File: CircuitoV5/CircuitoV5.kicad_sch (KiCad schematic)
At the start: 8 parts, among them U1 LM324

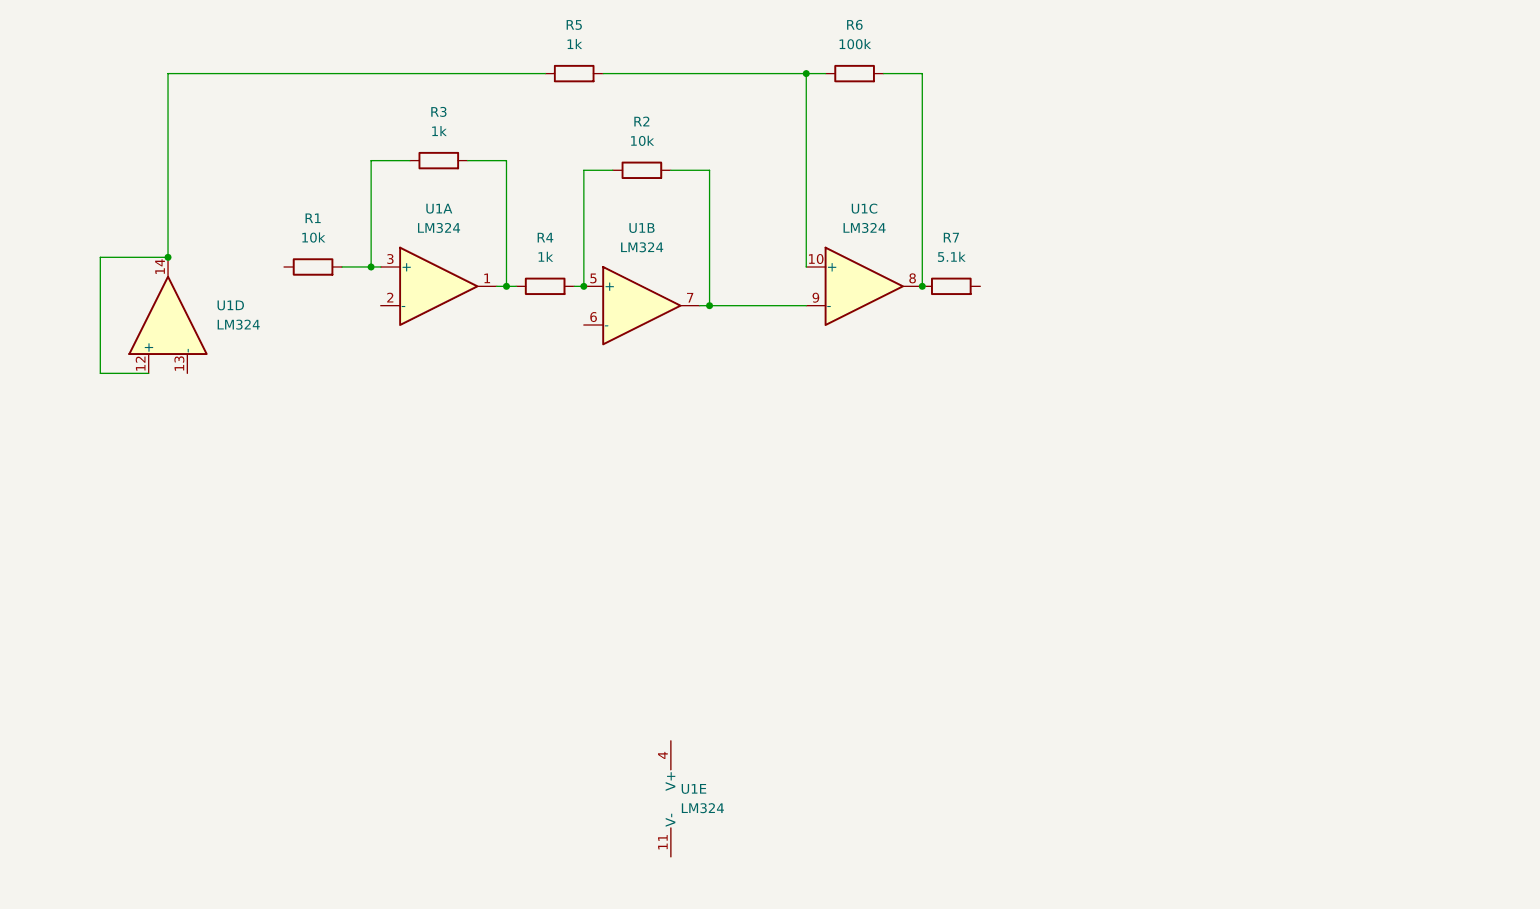
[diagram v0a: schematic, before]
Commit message: Schematic hecha, enrutado V1 planteado y empezado
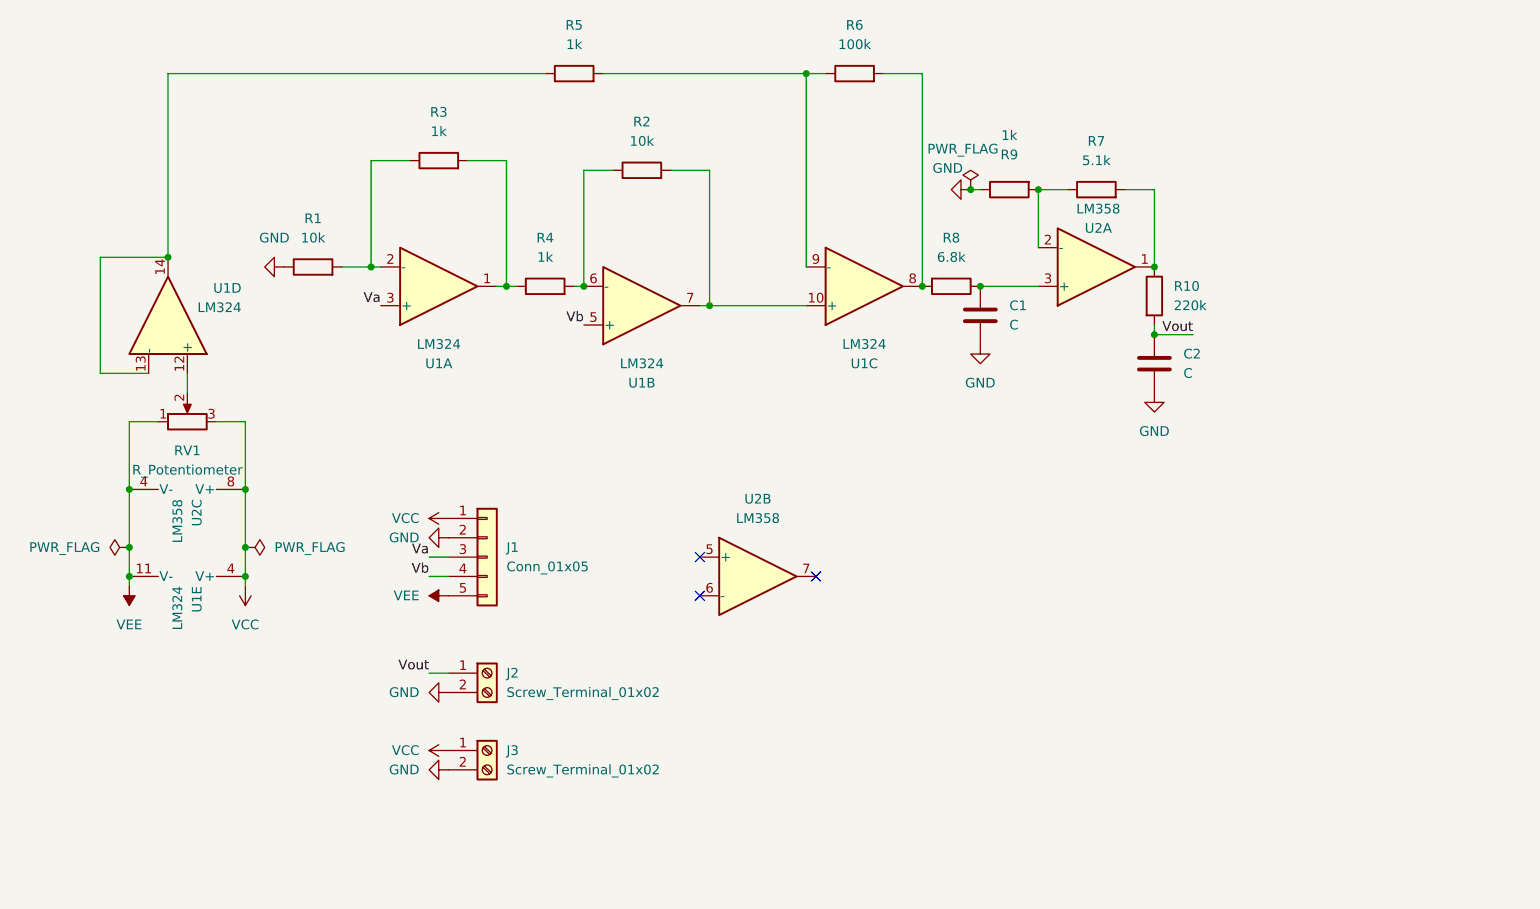
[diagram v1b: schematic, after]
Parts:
- added C1, C2: C, footprints:C_Rect_L9.5mm_W4.5mm_P5.00mm_MKT, symbol Device:C
- added J1: Conn_01x05, Connector_PinSocket_2.54mm:PinSocket_1x05_P2.54mm_Vertical, symbol Connector_Generic:Conn_01x05
- added J2, J3: Screw_Terminal_01x02, TerminalBlock_Phoenix:TerminalBlock_Phoenix_MKDS-1,5-2-5.08_1x02_P5.08mm_Horizontal, symbol Connector:Screw_Terminal_01x02
- added R10: 220k, Resistor_SMD:R_0201_0603Metric, symbol Device:R
- added R8: 6.8k, Resistor_SMD:R_0201_0603Metric, symbol Device:R
- added R9: 1k, Resistor_SMD:R_0603_1608Metric, symbol Device:R
- added RV1: R_Potentiometer, Potentiometer_THT:Potentiometer_Bourns_3296W_Vertical, symbol Device:R_Potentiometer
- added U2: LM358, footprints:DIP794W45P254L959H508Q8, symbol Amplifier_Operational:LM358
- U1: footprint (none) -> Package_SO:SOIC-14_3.9x8.7mm_P1.27mm; LCSC_Id C7943 -> C71035
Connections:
- net at R5.2, R6.1: now also U1.9 (-); no longer U1.10 (+)
- net at R6.2, U1.8: now also R8.2; no longer R7.1
- net at R2.2, U1.7: now also U1.10 (+); no longer U1.9 (-)
- net at U1.2 (-): now also R1.2, R3.1
- net at R5.1, U1.14: now also U1.13 (-); no longer U1.12 (+)
- net GND: now reaches R1.1
- net GND: now also C1.2, C2.2, J1.2 (Pin_2), J2.2 (Pin_2), J3.2 (Pin_2), R9.1
- net at R7.2: now also R10.1, U2.1
- net VEE: now reaches U1.11 (V-)
- net VEE: now also J1.5 (Pin_5), RV1.1, U2.4 (V-)
- net VCC: now reaches U1.4 (V+)
- net VCC: now also J1.1 (Pin_1), J3.1 (Pin_1), RV1.3, U2.8 (V+)
- net at R2.1, R4.2: now also U1.6 (-); no longer U1.5 (+)
- new net: R7.1, R9.2, U2.2 (-)
- new net: C1.1, R8.1, U2.3 (+)
- new net: RV1.2, U1.12 (+)
- new net Va: J1.3 (Pin_3), U1.3 (+)
- new net Vb: J1.4 (Pin_4), U1.5 (+)
- new net Vout: C2.1, J2.1 (Pin_1), R10.2
- no-connect marks 0 -> 3
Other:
- moved on the sheet: R7, U1D, U1E

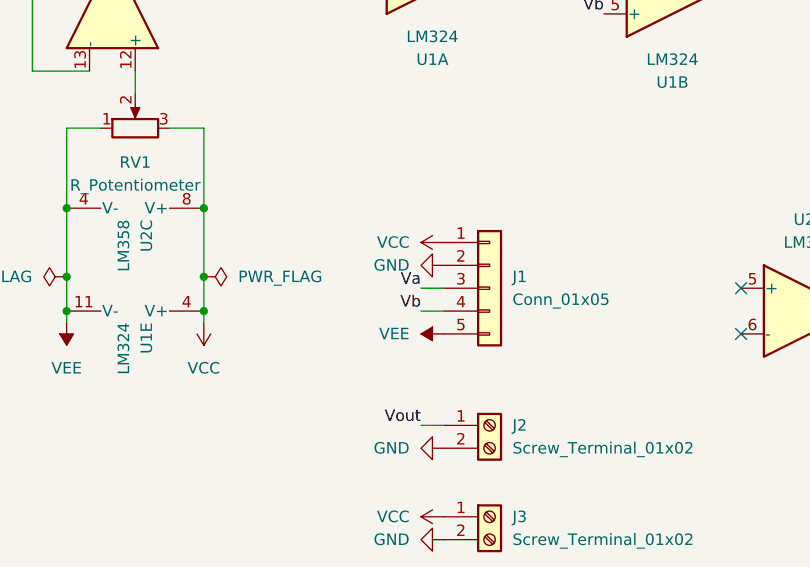
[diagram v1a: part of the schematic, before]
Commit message: componentes añadidos y proyecto ligeramente reordenado
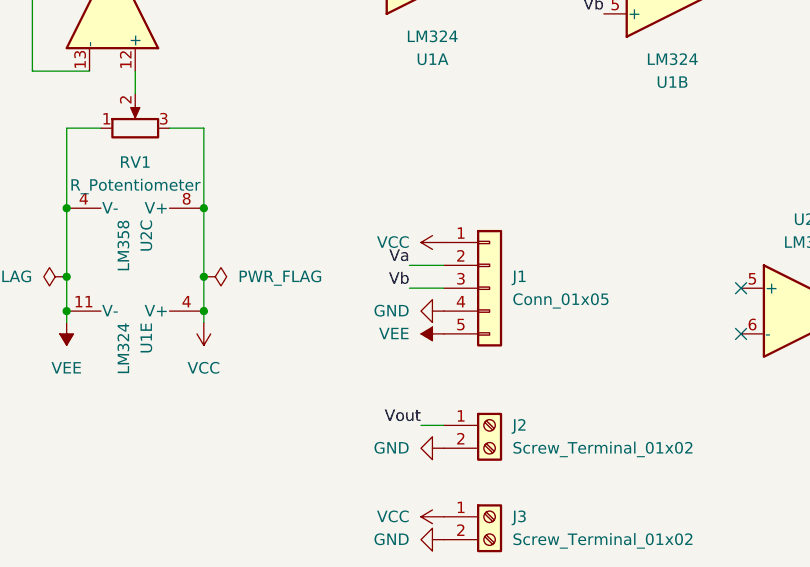
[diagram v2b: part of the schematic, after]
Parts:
- J1: footprint Connector_PinSocket_2.54mm:PinSocket_1x05_P2.54mm_Vertical -> Connector_PinSocket_2.54mm:PinSocket_1x05_P2.54mm_Horizontal
- U1: footprint Package_SO:SOIC-14_3.9x8.7mm_P1.27mm -> easyeda2kicad:PDIP-14_L19.7-W6.6-P2.54-LS8.3-BL
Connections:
- net GND: now also J1.4 (Pin_4); no longer J1.2 (Pin_2)
- net Va: now also J1.2 (Pin_2); no longer J1.3 (Pin_3)
- net Vb: now also J1.3 (Pin_3); no longer J1.4 (Pin_4)
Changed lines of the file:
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@@
 	(wire
 		(pts
-			(xy 86.36 91.44) (xy 88.9 91.44)
+			(xy 135.89 27.94) (xy 135.89 53.34)
 		)
 		(stroke
@@
 	(wire
 		(pts
-			(xy 135.89 27.94) (xy 135.89 53.34)
+			(xy 85.09 88.9) (xy 88.9 88.9)
 		)
 		(stroke
@@
 	(wire
 		(pts
-			(xy 135.89 58.42) (xy 123.19 58.42)
+			(xy 85.09 91.44) (xy 88.9 91.44)
 		)
 		(stroke
@@
 	(wire
 		(pts
-			(xy 105.41 55.88) (xy 106.68 55.88)
+			(xy 135.89 58.42) (xy 123.19 58.42)
 		)
 		(stroke
@@
 	(wire
 		(pts
-			(xy 62.23 82.55) (xy 62.23 90.17)
+			(xy 105.41 55.88) (xy 106.68 55.88)
 		)
 		(stroke
@@
 	(wire
 		(pts
-			(xy 46.99 82.55) (xy 46.99 90.17)
+			(xy 62.23 82.55) (xy 62.23 90.17)
 		)
 		(stroke
@@
 	(wire
 		(pts
-			(xy 166.37 43.18) (xy 166.37 50.8)
+			(xy 46.99 82.55) (xy 46.99 90.17)
 		)
 		(stroke
@@
 	(wire
 		(pts
-			(xy 78.74 53.34) (xy 80.01 53.34)
+			(xy 166.37 43.18) (xy 166.37 50.8)
 		)
 		(stroke
@@
 	(wire
 		(pts
-			(xy 91.44 39.37) (xy 96.52 39.37)
+			(xy 78.74 53.34) (xy 80.01 53.34)
 		)
 		(stroke
@@
 	(wire
 		(pts
-			(xy 54.61 67.31) (xy 54.61 69.85)
+			(xy 91.44 39.37) (xy 96.52 39.37)
 		)
 		(stroke
@@
 	(wire
 		(pts
-			(xy 86.36 93.98) (xy 88.9 93.98)
+			(xy 54.61 67.31) (xy 54.61 69.85)
 		)
 		(stroke
@@
 	)
 	(label "Vb"
-		(at 86.36 93.98 180)
+		(at 85.09 91.44 180)
 		(effects
 			(font
@@
 	)
 	(label "Va"
-		(at 86.36 91.44 180)
+		(at 85.09 88.9 180)
 		(effects
 			(font
@@
 			)
 		)
-		(property "Footprint" "Package_SO:SOIC-14_3.9x8.7mm_P1.27mm"
+		(property "Footprint" "easyeda2kicad:PDIP-14_L19.7-W6.6-P2.54-LS8.3-BL"
 			(at 142.24 58.42 0)
 			(hide yes)
@@
 			)
 		)
-		(property "Footprint" "Package_SO:SOIC-14_3.9x8.7mm_P1.27mm"
+		(property "Footprint" "easyeda2kicad:PDIP-14_L19.7-W6.6-P2.54-LS8.3-BL"
 			(at 86.36 58.42 0)
 			(hide yes)
@@
 			)
 		)
-		(property "Footprint" "Package_SO:SOIC-14_3.9x8.7mm_P1.27mm"
+		(property "Footprint" "easyeda2kicad:PDIP-14_L19.7-W6.6-P2.54-LS8.3-BL"
 			(at 54.61 60.96 0)
 			(hide yes)
@@
 	(symbol
 		(lib_id "power:GND")
-		(at 88.9 88.9 270)
+		(at 88.9 93.98 270)
 		(unit 1)
 		(body_style 1)
@@
 		(fields_autoplaced yes)
 		(property "Reference" "#PWR09"
-			(at 82.55 88.9 0)
+			(at 82.55 93.98 0)
 			(hide yes)
 			(show_name no)
@@
 		)
 		(property "Value" "GND"
-			(at 85.09 88.8999 90)
+			(at 85.09 93.9799 90)
 			(show_name no)
 			(do_not_autoplace no)
@@
 		)
 		(property "Footprint" ""
-			(at 88.9 88.9 0)
+			(at 88.9 93.98 0)
 			(hide yes)
 			(show_name no)
@@
 		)
 		(property "Datasheet" ""
-			(at 88.9 88.9 0)
+			(at 88.9 93.98 0)
 			(hide yes)
 			(show_name no)
@@
 		)
 		(property "Description" "Power symbol creates a global label with name \"GND\" , ground"
-			(at 88.9 88.9 0)
+			(at 88.9 93.98 0)
 			(hide yes)
 			(show_name no)
@@
 			)
 		)
-		(property "Footprint" "Package_SO:SOIC-14_3.9x8.7mm_P1.27mm"
+		(property "Footprint" "easyeda2kicad:PDIP-14_L19.7-W6.6-P2.54-LS8.3-BL"
 			(at 57.15 95.25 0)
 			(hide yes)
@@
 			)
 		)
-		(property "Footprint" "Package_SO:SOIC-14_3.9x8.7mm_P1.27mm"
+		(property "Footprint" "easyeda2kicad:PDIP-14_L19.7-W6.6-P2.54-LS8.3-BL"
 			(at 113.03 60.96 0)
 			(hide yes)
@@
 			)
 		)
-		(property "Footprint" "Connector_PinSocket_2.54mm:PinSocket_1x05_P2.54mm_Vertical"
+		(property "Footprint" "Connector_PinSocket_2.54mm:PinSocket_1x05_P2.54mm_Horizontal"
 			(at 93.98 91.44 0)
 			(hide yes)

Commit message: Routed and done
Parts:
- removed J2, J3: Screw_Terminal_01x02, TerminalBlock_Phoenix:TerminalBlock_Phoenix_MKDS-1,5-2-5.08_1x02_P5.08mm_Horizontal, symbol Connector:Screw_Terminal_01x02
- added C3, C4: LM324, Capacitor_THT:C_Disc_D5.0mm_W2.5mm_P2.50mm, symbol Device:C
- added C5, C6: LM358, Capacitor_THT:C_Disc_D5.0mm_W2.5mm_P2.50mm, symbol Device:C
- added J2, J3: Conn_01x02, Connector_PinSocket_2.54mm:PinSocket_1x02_P2.54mm_Vertical, symbol Connector_Generic:Conn_01x02
- R1, R2, R7: footprint Resistor_SMD:R_0402_1005Metric -> Resistor_THT:R_Axial_DIN0207_L6.3mm_D2.5mm_P10.16mm_Horizontal
- R10, R8: footprint Resistor_SMD:R_0201_0603Metric -> Resistor_THT:R_Axial_DIN0207_L6.3mm_D2.5mm_P10.16mm_Horizontal
- R3, R4, R5, R6, R9: footprint Resistor_SMD:R_0603_1608Metric -> Resistor_THT:R_Axial_DIN0207_L6.3mm_D2.5mm_P10.16mm_Horizontal
- U1: footprint easyeda2kicad:PDIP-14_L19.7-W6.6-P2.54-LS8.3-BL -> Package_DIP:DIP-14_W7.62mm
- U2: footprint footprints:DIP794W45P254L959H508Q8 -> Package_DIP:DIP-8_W7.62mm
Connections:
- net GND: now also C3.2, C4.2, C5.2, C6.2, J2.2 (Pin_2), J3.2 (Pin_2)
- net VCC: now also C3.1, C5.1, J3.1 (Pin_1)
- net VEE: now also C4.1, C6.1
- net Vout: now also U2.6 (-), U2.7, J2.1 (Pin_1); no longer C2.1, R10.2
- net at R10.1, R7.2, U2.1: now also U2.5 (+)
- new net: C2.1, R10.2
- no-connect marks 3 -> 0
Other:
- moved on the sheet: C2, J1, U2B
